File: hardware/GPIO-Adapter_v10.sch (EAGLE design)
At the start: 8 parts, among them J1 FPC40_PIN, X1 PASSER, X2 PASSER, X3 PASSER, X4 PASSER

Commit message: updated docu and schematics
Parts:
- renumbered J1 to J1-TOP

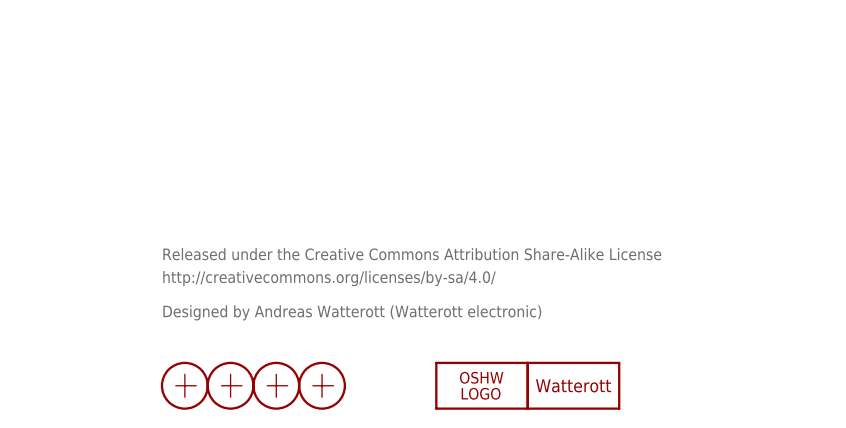
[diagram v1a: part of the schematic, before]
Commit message: updated schematics
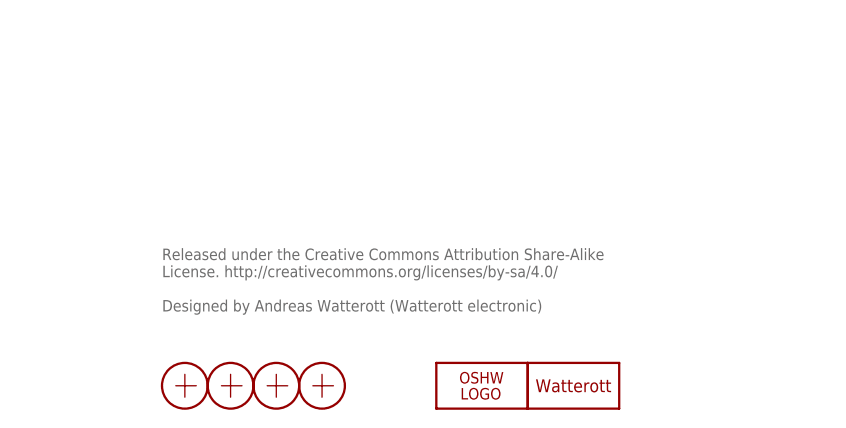
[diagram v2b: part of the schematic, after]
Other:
- note added: "Released under the Creative Commons Attribution Share-Alike License. http://creativecommons.org/licenses/by-sa/4.0/ Designed by Andreas Watterott (Watterott electronic)"
- note removed: "Designed by Andreas Watterott (Watterott electronic)"
- note removed: "Released under the Creative Commons Attribution Share-Alike License"
- note removed: "http://creativecommons.org/licenses/by-sa/4.0/"
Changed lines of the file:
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@@
 <setting verticaltext="up"/>
 </settings>
-<grid distance="0.1" unitdist="inch" unit="inch" style="lines" multiple="1" display="no" altdistance="0.01" altunitdist="inch" altunit="inch"/>
+<grid distance="0.05" unitdist="inch" unit="inch" style="lines" multiple="1" display="yes" altdistance="0.025" altunitdist="inch" altunit="inch"/>
 <layers>
-<layer number="1" name="Top" color="4" fill="1" visible="yes" active="no"/>
-<layer number="2" name="Route2" color="1" fill="3" visible="yes" active="no"/>
-<layer number="3" name="Route3" color="4" fill="3" visible="yes" active="no"/>
-<layer number="4" name="Route4" color="1" fill="4" visible="yes" active="no"/>
-<layer number="5" name="Route5" color="4" fill="4" visible="yes" active="no"/>
-<layer number="6" name="Route6" color="1" fill="8" visible="yes" active="no"/>
-<layer number="7" name="Route7" color="4" fill="8" visible="yes" active="no"/>
-<layer number="8" name="Route8" color="1" fill="2" visible="yes" active="no"/>
-<layer number="9" name="Route9" color="4" fill="2" visible="yes" active="no"/>
-<layer number="10" name="Route10" color="1" fill="7" visible="yes" active="no"/>
-<layer number="11" name="Route11" color="4" fill="7" visible="yes" active="no"/>
-<layer number="12" name="Route12" color="1" fill="5" visible="yes" active="no"/>
-<layer number="13" name="Route13" color="4" fill="5" visible="yes" active="no"/>
-<layer number="14" name="Route14" color="1" fill="6" visible="yes" active="no"/>
-<layer number="15" name="Route15" color="4" fill="6" visible="yes" active="no"/>
-<layer number="16" name="Bottom" color="1" fill="1" visible="yes" active="no"/>
-<layer number="17" name="Pads" color="2" fill="1" visible="yes" active="no"/>
-<layer number="18" name="Vias" color="2" fill="1" visible="yes" active="no"/>
-<layer number="19" name="Unrouted" color="6" fill="1" visible="yes" active="no"/>
-<layer number="20" name="Dimension" color="15" fill="1" visible="yes" active="no"/>
-<layer number="21" name="tPlace" color="7" fill="1" visible="yes" active="no"/>
-<layer number="22" name="bPlace" color="7" fill="1" visible="yes" active="no"/>
-<layer number="23" name="tOrigins" color="15" fill="1" visible="yes" active="no"/>
-<layer number="24" name="bOrigins" color="15" fill="1" visible="yes" active="no"/>
-<layer number="25" name="tNames" color="7" fill="1" visible="yes" active="no"/>
-<layer number="26" name="bNames" color="7" fill="1" visible="yes" active="no"/>
-<layer number="27" name="tValues" color="7" fill="1" visible="yes" active="no"/>
-<layer number="28" name="bValues" color="7" fill="1" visible="yes" active="no"/>
+<layer number="1" name="Top" color="4" fill="1" visible="no" active="no"/>
+<layer number="2" name="Route2" color="1" fill="3" visible="no" active="no"/>
+<layer number="3" name="Route3" color="4" fill="3" visible="no" active="no"/>
+<layer number="4" name="Route4" color="1" fill="4" visible="no" active="no"/>
+<layer number="5" name="Route5" color="4" fill="4" visible="no" active="no"/>
+<layer number="6" name="Route6" color="1" fill="8" visible="no" active="no"/>
+<layer number="7" name="Route7" color="4" fill="8" visible="no" active="no"/>
+<layer number="8" name="Route8" color="1" fill="2" visible="no" active="no"/>
+<layer number="9" name="Route9" color="4" fill="2" visible="no" active="no"/>
+<layer number="10" name="Route10" color="1" fill="7" visible="no" active="no"/>
+<layer number="11" name="Route11" color="4" fill="7" visible="no" active="no"/>
+<layer number="12" name="Route12" color="1" fill="5" visible="no" active="no"/>
+<layer number="13" name="Route13" color="4" fill="5" visible="no" active="no"/>
+<layer number="14" name="Route14" color="1" fill="6" visible="no" active="no"/>
+<layer number="15" name="Route15" color="4" fill="6" visible="no" active="no"/>
+<layer number="16" name="Bottom" color="1" fill="1" visible="no" active="no"/>
+<layer number="17" name="Pads" color="2" fill="1" visible="no" active="no"/>
+<layer number="18" name="Vias" color="2" fill="1" visible="no" active="no"/>
+<layer number="19" name="Unrouted" color="6" fill="1" visible="no" active="no"/>
+<layer number="20" name="Dimension" color="15" fill="1" visible="no" active="no"/>
+<layer number="21" name="tPlace" color="7" fill="1" visible="no" active="no"/>
+<layer number="22" name="bPlace" color="7" fill="1" visible="no" active="no"/>
+<layer number="23" name="tOrigins" color="15" fill="1" visible="no" active="no"/>
+<layer number="24" name="bOrigins" color="15" fill="1" visible="no" active="no"/>
+<layer number="25" name="tNames" color="7" fill="1" visible="no" active="no"/>
+<layer number="26" name="bNames" color="7" fill="1" visible="no" active="no"/>
+<layer number="27" name="tValues" color="7" fill="1" visible="no" active="no"/>
+<layer number="28" name="bValues" color="7" fill="1" visible="no" active="no"/>
 <layer number="29" name="tStop" color="7" fill="3" visible="no" active="no"/>
 <layer number="30" name="bStop" color="7" fill="6" visible="no" active="no"/>
@@
 <layer number="35" name="tGlue" color="7" fill="4" visible="no" active="no"/>
 <layer number="36" name="bGlue" color="7" fill="5" visible="no" active="no"/>
-<layer number="37" name="tTest" color="7" fill="1" visible="yes" active="no"/>
-<layer number="38" name="bTest" color="7" fill="1" visible="yes" active="no"/>
+<layer number="37" name="tTest" color="7" fill="1" visible="no" active="no"/>
+<layer number="38" name="bTest" color="7" fill="1" visible="no" active="no"/>
 <layer number="39" name="tKeepout" color="4" fill="11" visible="no" active="no"/>
 <layer number="40" name="bKeepout" color="1" fill="11" visible="no" active="no"/>
@@
 <layer number="44" name="Drills" color="7" fill="1" visible="no" active="no"/>
 <layer number="45" name="Holes" color="7" fill="1" visible="no" active="no"/>
-<layer number="46" name="Milling" color="3" fill="1" visible="yes" active="no"/>
-<layer number="47" name="Measures" color="7" fill="1" visible="yes" active="no"/>
-<layer number="48" name="Document" color="7" fill="1" visible="yes" active="no"/>
-<layer number="49" name="Reference" color="7" fill="1" visible="yes" active="no"/>
-<layer number="50" name="dxf" color="7" fill="1" visible="yes" active="no"/>
-<layer number="51" name="tDocu" color="7" fill="1" visible="yes" active="no"/>
-<layer number="52" name="bDocu" color="7" fill="1" visible="yes" active="no"/>
-<layer number="53" name="tCopper" color="7" fill="11" visible="yes" active="no"/>
-<layer number="54" name="bCopper" color="7" fill="1" visible="yes" active="no"/>
-<layer number="56" name="wert" color="7" fill="1" visible="yes" active="no"/>
-<layer number="57" name="tCAD" color="7" fill="1" visible="yes" active="no"/>
+<layer number="46" name="Milling" color="3" fill="1" visible="no" active="no"/>
+<layer number="47" name="Measures" color="7" fill="1" visible="no" active="no"/>
+<layer number="48" name="Document" color="7" fill="1" visible="no" active="no"/>
+<layer number="49" name="Reference" color="7" fill="1" visible="no" active="no"/>
+<layer number="50" name="dxf" color="7" fill="1" visible="no" active="no"/>
+<layer number="51" name="tDocu" color="7" fill="1" visible="no" active="no"/>
+<layer number="52" name="bDocu" color="7" fill="1" visible="no" active="no"/>
 <layer number="90" name="Modules" color="5" fill="1" visible="yes" active="yes"/>
 <layer number="91" name="Nets" color="2" fill="1" visible="yes" active="yes"/>
@@
 <layer number="98" name="Guide" color="6" fill="1" visible="yes" active="yes"/>
 <layer number="99" name="SpiceOrder" color="5" fill="1" visible="yes" active="yes"/>
-<layer number="100" name="Muster" color="7" fill="1" visible="no" active="no"/>
-<layer number="153" name="FabDoc1" color="6" fill="1" visible="no" active="no"/>
-<layer number="154" name="FabDoc2" color="2" fill="1" visible="no" active="no"/>
-<layer number="155" name="FabDoc3" color="7" fill="15" visible="no" active="no"/>
-<layer number="217" name="217bmp" color="18" fill="1" visible="no" active="no"/>
-<layer number="218" name="218bmp" color="19" fill="1" visible="no" active="no"/>
-<layer number="219" name="219bmp" color="20" fill="1" visible="no" active="no"/>
-<layer number="220" name="220bmp" color="21" fill="1" visible="no" active="no"/>
-<layer number="221" name="221bmp" color="22" fill="1" visible="no" active="no"/>
-<layer number="222" name="222bmp" color="23" fill="1" visible="no" active="no"/>
-<layer number="223" name="223bmp" color="24" fill="1" visible="no" active="no"/>
-<layer number="224" name="224bmp" color="25" fill="1" visible="no" active="no"/>
-<layer number="251" name="SMDround" color="12" fill="11" visible="no" active="no"/>
 </layers>
 <schematic xreflabel="%F%N/%S.%C%R" xrefpart="/%S.%C%R">
@@
 <sheet>
 <plain>
-<text x="162.56" y="21.59" size="1.27" layer="95">Released under the Creative Commons Attribution Share-Alike License</text>
-<text x="162.56" y="19.05" size="1.27" layer="95">http://creativecommons.org/licenses/by-sa/4.0/</text>
-<text x="162.56" y="15.24" size="1.27" layer="95">Designed by Andreas Watterott (Watterott electronic)</text>
+<text x="162.56" y="22.86" size="1.27" layer="95" align="top-left">Released under the Creative Commons Attribution Share-Alike
+License. http://creativecommons.org/licenses/by-sa/4.0/
+Designed by Andreas Watterott (Watterott electronic)</text>
 </plain>
 <instances>
@@
 </schematic>
 </drawing>
+<compatibility>
+<note version="6.3" minversion="6.2.2" severity="warning">
+Since Version 6.2.2 text objects can contain more than one line,
+which will not be processed correctly with this version.
+</note>
+</compatibility>
 </eagle>

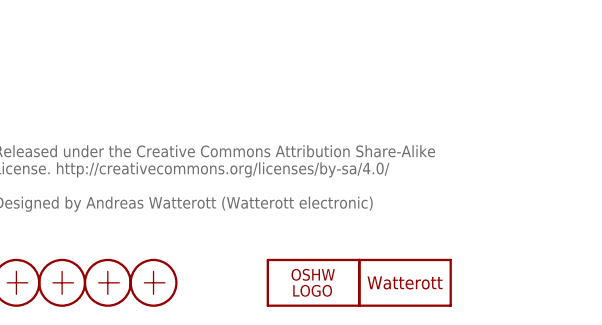
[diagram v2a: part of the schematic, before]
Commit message: updated schematics
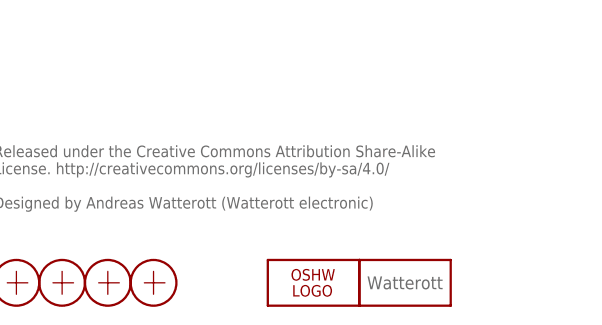
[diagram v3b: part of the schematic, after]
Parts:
- removed LOGO2: LOGO-S_PLACE_M, we-symbol:LOGO-S_PLACE_M
- added LOGO3: LOGO_SPARK-4, we-symbol:LOGO_SPARK-4
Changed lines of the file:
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@@
 <?xml version="1.0" encoding="utf-8"?>
 <!DOCTYPE eagle SYSTEM "eagle.dtd">
-<eagle version="7.5.0">
+<eagle version="7.7.0">
 <drawing>
 <settings>
@@
 <setting verticaltext="up"/>
 </settings>
-<grid distance="0.05" unitdist="inch" unit="inch" style="lines" multiple="1" display="yes" altdistance="0.025" altunitdist="inch" altunit="inch"/>
+<grid distance="0.05" unitdist="inch" unit="inch" style="lines" multiple="1" display="yes" altdistance="0.01" altunitdist="inch" altunit="inch"/>
 <layers>
 <layer number="1" name="Top" color="4" fill="1" visible="no" active="no"/>
@@
 <part name="RPI" library="we-board" deviceset="RPI_B+" device="-CON" value="RPI"/>
 <part name="J1-TOP" library="we-con" deviceset="FPC40_PIN" device=""/>
-<part name="LOGO2" library="we-symbol" deviceset="LOGO" device="-S_PLACE_M" value="LOGO-S_PLACE_M"/>
 <part name="FRAME1" library="we-symbol" deviceset="FRAME-A4L" device=""/>
+<part name="LOGO3" library="we-symbol" deviceset="LOGO_SPARK" device="-4"/>
 </parts>
 <sheets>
@@
 <instance part="LOGO1" gate="G$1" x="198.12" y="7.62"/>
 <instance part="RPI" gate="RPI" x="128.27" y="99.06"/>
-<instance part="LOGO2" gate="L" x="208.28" y="7.62"/>
 <instance part="J1-TOP" gate="P40" x="148.59" y="73.66"/>
 <instance part="J1-TOP" gate="P1" x="107.95" y="121.92" rot="R180"/>
@@
 <instance part="J1-TOP" gate="P39" x="107.95" y="73.66" rot="R180"/>
 <instance part="FRAME1" gate="F" x="0" y="0"/>
+<instance part="LOGO3" gate="G$1" x="208.28" y="7.62"/>
 </instances>
 <busses>
